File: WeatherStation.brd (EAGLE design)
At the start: 30.5 x 53.3 mm, 35 parts, among them J1 EDISON_CONNECTOR_FULLMOUNTING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, J2 EDISON_CONNECTOR_FULLHEADER, U1 MCP73831, U2 HTU21DSMD, U3 MPL3115A2LGA8, U4 PCA9306

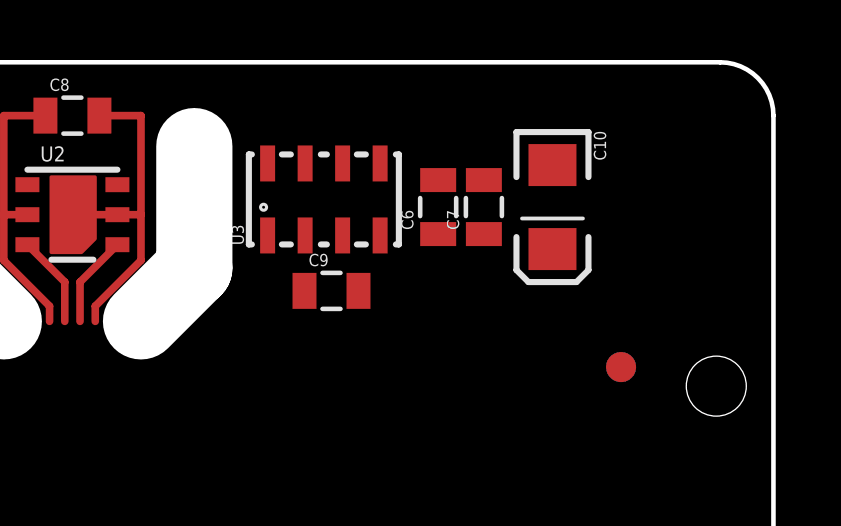
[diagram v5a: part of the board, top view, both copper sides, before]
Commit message: set and drew traces for MPL3115A2
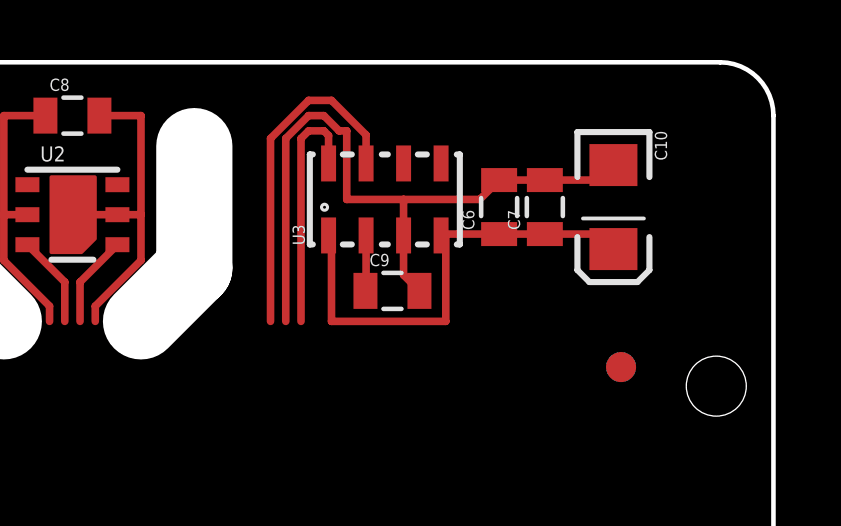
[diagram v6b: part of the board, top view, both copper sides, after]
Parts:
- moved C9 2.03 mm to (17.8, 45.7)
- moved C10 2.03 mm to (25.1, 48.5)
- moved C6 2.03 mm to (21.3, 48.5)
- moved C7 2.03 mm to (22.9, 48.5)
- moved U3 2.03 mm to (17.5, 48.8)
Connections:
- removed net N$10: U3.7
- removed net N$9: U3.8
- net SCL: now also U3.8
- net SDA: now also U3.7
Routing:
- net GND: track 11.2 -> 34.7 mm
- net 3.3V: track 15.7 -> 31.4 mm
- net SDA: track 3.07 -> 14.3 mm
- net SCL: track 3.07 -> 11.2 mm
- net N$3: track 0.00 -> 1.86 mm
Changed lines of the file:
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@@
 <element name="JP2" library="SparkFun-Connectors" package="1X02" value="M02PTH" x="2.032" y="22.098" smashed="yes" rot="R270"/>
 <element name="U2" library="SparkFun-Sensors" package="HTU21D" value="HTU21DSMD" x="7.112" y="48.26"/>
-<element name="U3" library="SparkFun-Sensors" package="LGA8" value="MPL3115A2LGA8" x="15.494" y="48.768" rot="R90"/>
+<element name="U3" library="SparkFun-Sensors" package="LGA8" value="MPL3115A2LGA8" x="17.526" y="48.768" rot="R90"/>
 <element name="U4" library="SparkFun-DigitalIC" package="PSOP-8" value="PCA9306" x="12.954" y="35.052">
 <attribute name="PROD_ID" value="IC-10023" x="12.954" y="35.052" size="1.778" layer="27" display="off"/>
@@
 <element name="C4" library="SparkFun-Capacitors" package="0805" value="4.7µF" x="11.176" y="27.94"/>
 <element name="C5" library="SparkFun-Capacitors" package="0805" value="4.7µF" x="14.986" y="25.4" rot="R90"/>
-<element name="C6" library="SparkFun-Capacitors" package="0805" value="0.1µF" x="19.304" y="48.514" rot="R90"/>
-<element name="C7" library="SparkFun-Capacitors" package="0805" value="1µF" x="20.828" y="48.514" rot="R90"/>
+<element name="C6" library="SparkFun-Capacitors" package="0805" value="0.1µF" x="21.336" y="48.514" rot="R90"/>
+<element name="C7" library="SparkFun-Capacitors" package="0805" value="1µF" x="22.86" y="48.514" rot="R90"/>
 <element name="R3" library="SparkFun-Resistors" package="0603-RES" value="330Ω" x="-33.782" y="-16.51"/>
 <element name="R4" library="SparkFun-Resistors" package="0603-RES" value="330Ω" x="-33.782" y="-19.558"/>
@@
 <element name="R7" library="SparkFun-Resistors" package="0603-RES" value="330Ω" x="-33.782" y="-28.702"/>
 <element name="C8" library="SparkFun-Capacitors" package="0805" value="4.7µF" x="7.112" y="51.562"/>
-<element name="C9" library="SparkFun-Capacitors" package="0805" value="0.1µF" x="15.748" y="45.72"/>
-<element name="C10" library="SparkFun-Capacitors" package="EIA3216" value="10µF" x="23.114" y="48.514" rot="R270"/>
+<element name="C9" library="SparkFun-Capacitors" package="0805" value="0.1µF" x="17.78" y="45.72"/>
+<element name="C10" library="SparkFun-Capacitors" package="EIA3216" value="10µF" x="25.146" y="48.514" rot="R270"/>
 </elements>
 <signals>
@@
 <wire x1="7.874" y1="45.212" x2="7.874" y2="44.704" width="0.254" layer="1"/>
 <wire x1="8.612" y1="48.26" x2="9.398" y2="48.26" width="0.254" layer="1"/>
-<wire x1="20.828" y1="49.414" x2="23.114" y2="49.914" width="0" layer="19" extent="1-1"/>
-<wire x1="19.304" y1="49.414" x2="20.828" y2="49.414" width="0" layer="19" extent="1-1"/>
-<wire x1="16.119" y1="47.568" x2="19.304" y2="49.414" width="0" layer="19" extent="1-1"/>
-<wire x1="16.648" y1="45.72" x2="16.119" y2="47.568" width="0" layer="19" extent="1-1"/>
-<wire x1="9.398" y1="48.26" x2="16.119" y2="47.568" width="0" layer="19" extent="1-1"/>
-<wire x1="13.724" y1="33.682" x2="16.648" y2="45.72" width="0" layer="19" extent="1-1"/>
+<wire x1="8.612" y1="48.26" x2="7.112" y2="48.26" width="0.254" layer="1"/>
+<wire x1="18.68" y1="45.72" x2="18.151" y2="46.249" width="0.254" layer="1"/>
+<wire x1="18.151" y1="46.249" x2="18.151" y2="47.568" width="0.254" layer="1"/>
+<wire x1="18.151" y1="47.568" x2="18.151" y2="48.768" width="0.254" layer="1"/>
+<wire x1="18.151" y1="48.768" x2="20.69" y2="48.768" width="0.254" layer="1"/>
+<wire x1="20.69" y1="48.768" x2="21.336" y2="49.414" width="0.254" layer="1"/>
+<wire x1="13.724" y1="33.682" x2="18.68" y2="45.72" width="0" layer="19" extent="1-1"/>
 <wire x1="12.076" y1="27.94" x2="13.724" y2="33.682" width="0" layer="19" extent="1-1"/>
 <wire x1="14.986" y1="26.3" x2="12.076" y2="27.94" width="0" layer="19" extent="1-1"/>
@@
 <wire x1="27.1272" y1="20.5232" x2="25.96" y2="20.58" width="0" layer="19" extent="16-16"/>
 <wire x1="28.2448" y1="22.1742" x2="26.9438" y2="22.1798" width="0" layer="19" extent="1-1"/>
-<wire x1="8.612" y1="48.26" x2="7.112" y2="48.26" width="0.254" layer="1"/>
+<wire x1="22.86" y1="49.414" x2="21.336" y2="49.414" width="0.254" layer="1"/>
+<wire x1="22.86" y1="49.414" x2="24.646" y2="49.414" width="0.254" layer="1"/>
+<wire x1="24.646" y1="49.414" x2="25.146" y2="49.914" width="0.254" layer="1"/>
+<wire x1="14.986" y1="48.768" x2="14.986" y2="44.704" width="0" layer="19" extent="1-16"/>
+<wire x1="14.986" y1="44.704" x2="9.398" y2="46.736" width="0" layer="19" extent="1-16"/>
+<wire x1="18.151" y1="48.768" x2="16.256" y2="48.768" width="0.254" layer="1"/>
+<wire x1="16.256" y1="48.768" x2="16.256" y2="51.054" width="0.254" layer="1"/>
+<wire x1="16.256" y1="51.054" x2="16.002" y2="51.054" width="0.254" layer="1"/>
+<wire x1="16.002" y1="51.054" x2="15.494" y2="51.562" width="0.254" layer="1"/>
+<wire x1="15.494" y1="51.562" x2="14.986" y2="51.562" width="0.254" layer="1"/>
+<wire x1="14.986" y1="51.562" x2="14.224" y2="50.8" width="0.254" layer="1"/>
+<wire x1="14.224" y1="50.8" x2="14.224" y2="44.704" width="0.254" layer="1"/>
+<wire x1="14.224" y1="44.704" x2="9.398" y2="46.736" width="0" layer="19" extent="1-16"/>
 </signal>
 <signal name="VSYS">
@@
 <wire x1="4.826" y1="46.736" x2="6.35" y2="45.212" width="0.254" layer="1"/>
 <wire x1="5.612" y1="48.26" x2="4.826" y2="48.26" width="0.254" layer="1"/>
-<wire x1="20.828" y1="47.614" x2="23.114" y2="47.114" width="0" layer="19" extent="1-1"/>
-<wire x1="19.304" y1="47.614" x2="20.828" y2="47.614" width="0" layer="19" extent="1-1"/>
-<wire x1="17.369" y1="47.568" x2="19.304" y2="47.614" width="0" layer="19" extent="1-1"/>
-<wire x1="13.619" y1="47.568" x2="17.369" y2="47.568" width="0" layer="19" extent="1-1"/>
-<wire x1="6.096" y1="45.466" x2="13.619" y2="47.568" width="0" layer="19" extent="1-1"/>
+<wire x1="6.35" y1="45.212" x2="6.35" y2="44.704" width="0.254" layer="1"/>
+<wire x1="19.401" y1="47.568" x2="19.447" y2="47.614" width="0.254" layer="1"/>
+<wire x1="19.447" y1="47.614" x2="21.336" y2="47.614" width="0.254" layer="1"/>
+<wire x1="21.336" y1="47.614" x2="22.86" y2="47.614" width="0.254" layer="1"/>
+<wire x1="22.86" y1="47.614" x2="24.646" y2="47.614" width="0.254" layer="1"/>
+<wire x1="24.646" y1="47.614" x2="25.146" y2="47.114" width="0.254" layer="1" curve="-90"/>
+<wire x1="15.651" y1="47.568" x2="15.748" y2="47.471" width="0.254" layer="1"/>
+<wire x1="15.748" y1="47.471" x2="15.748" y2="44.704" width="0.254" layer="1"/>
+<wire x1="15.748" y1="44.704" x2="19.558" y2="44.704" width="0.254" layer="1"/>
+<wire x1="19.558" y1="44.704" x2="19.558" y2="47.568" width="0.254" layer="1"/>
+<wire x1="19.558" y1="47.568" x2="19.401" y2="47.568" width="0.254" layer="1"/>
+<wire x1="6.35" y1="44.704" x2="15.748" y2="44.704" width="0" layer="19" extent="1-1"/>
+<wire x1="10.276" y1="27.94" x2="15.748" y2="44.704" width="0" layer="19" extent="1-1"/>
 <wire x1="12.4761" y1="26.35" x2="10.276" y2="27.94" width="0" layer="19" extent="1-1"/>
 <wire x1="21.717" y1="22.0472" x2="12.4761" y2="26.35" width="0" layer="19" extent="1-1"/>
-<wire x1="6.096" y1="45.466" x2="6.35" y2="45.212" width="0" layer="19" extent="1-16"/>
-<wire x1="6.35" y1="45.212" x2="6.35" y2="44.704" width="0.254" layer="1"/>
-<wire x1="6.35" y1="44.704" x2="13.619" y2="47.568" width="0" layer="19" extent="1-16"/>
 </signal>
 <signal name="GP183_PWM3">
@@
 <wire x1="8.612" y1="47.26" x2="7.366" y2="46.014" width="0.254" layer="1"/>
 <wire x1="7.366" y1="46.014" x2="7.366" y2="44.704" width="0.254" layer="1"/>
-<wire x1="7.366" y1="44.704" x2="13.224" y2="33.682" width="0" layer="19" extent="1-16"/>
+<contactref element="U3" pad="7"/>
+<wire x1="13.224" y1="33.682" x2="7.366" y2="44.704" width="0" layer="19" extent="1-1"/>
+<wire x1="16.901" y1="49.968" x2="16.901" y2="50.917" width="0.254" layer="1"/>
+<wire x1="16.901" y1="50.917" x2="15.748" y2="52.07" width="0.254" layer="1"/>
+<wire x1="15.748" y1="52.07" x2="14.986" y2="52.07" width="0.254" layer="1"/>
+<wire x1="14.986" y1="52.07" x2="13.716" y2="50.8" width="0.254" layer="1"/>
+<wire x1="13.716" y1="50.8" x2="13.716" y2="44.704" width="0.254" layer="1"/>
+<wire x1="13.716" y1="44.704" x2="8.612" y2="47.26" width="0" layer="19" extent="1-16"/>
 </signal>
 <signal name="SCL">
@@
 <wire x1="5.612" y1="47.26" x2="6.858" y2="46.014" width="0.254" layer="1"/>
 <wire x1="6.858" y1="46.014" x2="6.858" y2="44.704" width="0.254" layer="1"/>
-<wire x1="6.858" y1="44.704" x2="12.724" y2="33.682" width="0" layer="19" extent="1-16"/>
+<contactref element="U3" pad="8"/>
+<wire x1="12.724" y1="33.682" x2="6.858" y2="44.704" width="0" layer="19" extent="1-1"/>
+<wire x1="15.651" y1="49.968" x2="15.651" y2="50.897" width="0.254" layer="1"/>
+<wire x1="15.651" y1="50.897" x2="15.494" y2="51.054" width="0.254" layer="1"/>
+<wire x1="15.494" y1="51.054" x2="14.986" y2="51.054" width="0.254" layer="1"/>
+<wire x1="14.986" y1="51.054" x2="14.732" y2="50.8" width="0.254" layer="1"/>
+<wire x1="14.732" y1="50.8" x2="14.732" y2="44.704" width="0.254" layer="1"/>
+<wire x1="14.732" y1="44.704" x2="6.858" y2="44.704" width="0" layer="19" extent="1-16"/>
 </signal>
 <signal name="N$3">
 <contactref element="U3" pad="2"/>
 <contactref element="C9" pad="1"/>
-<wire x1="14.869" y1="47.568" x2="14.848" y2="45.72" width="0" layer="19" extent="1-1"/>
-</signal>
-<signal name="N$9">
-<contactref element="U3" pad="8"/>
-</signal>
-<signal name="N$10">
-<contactref element="U3" pad="7"/>
+<wire x1="16.88" y1="45.72" x2="16.901" y2="45.741" width="0.254" layer="1"/>
+<wire x1="16.901" y1="45.741" x2="16.901" y2="47.568" width="0.254" layer="1"/>
 </signal>
 </signals>

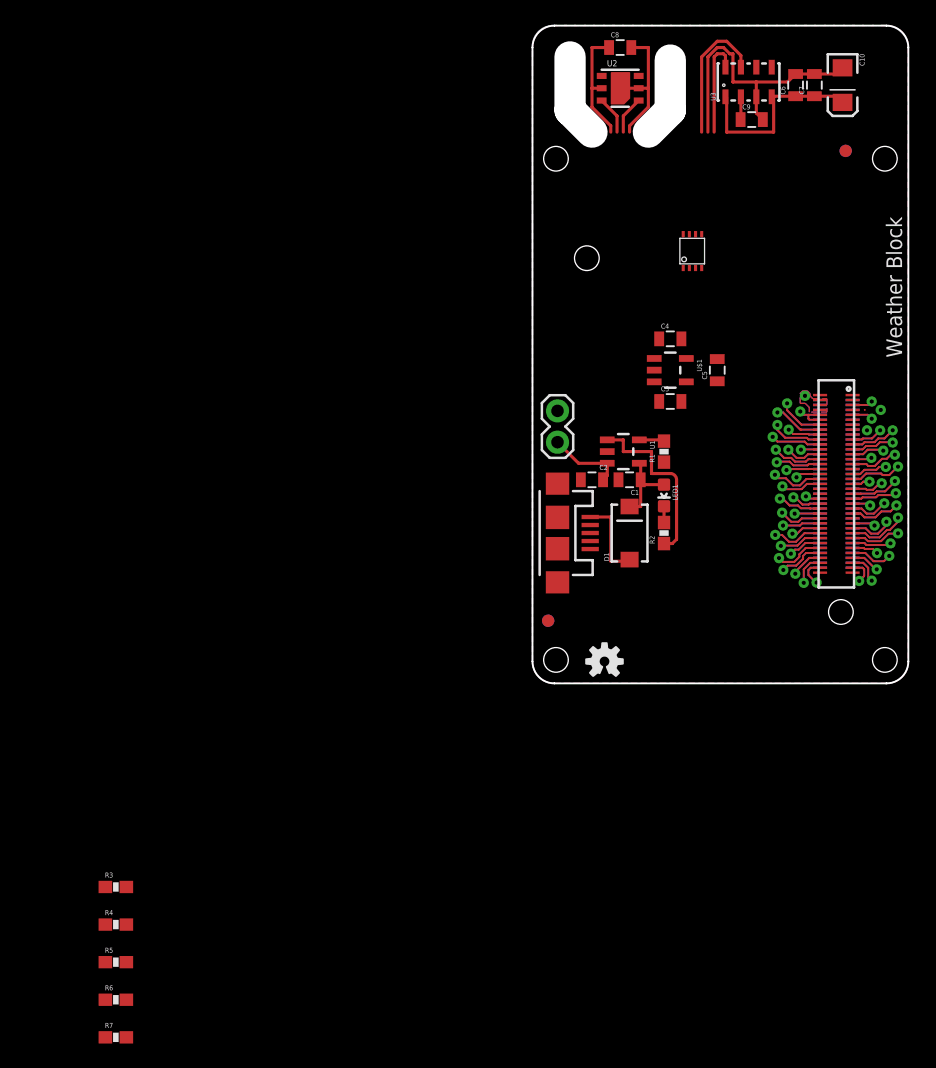
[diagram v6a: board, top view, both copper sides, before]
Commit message: set and drew traces for MIC5205
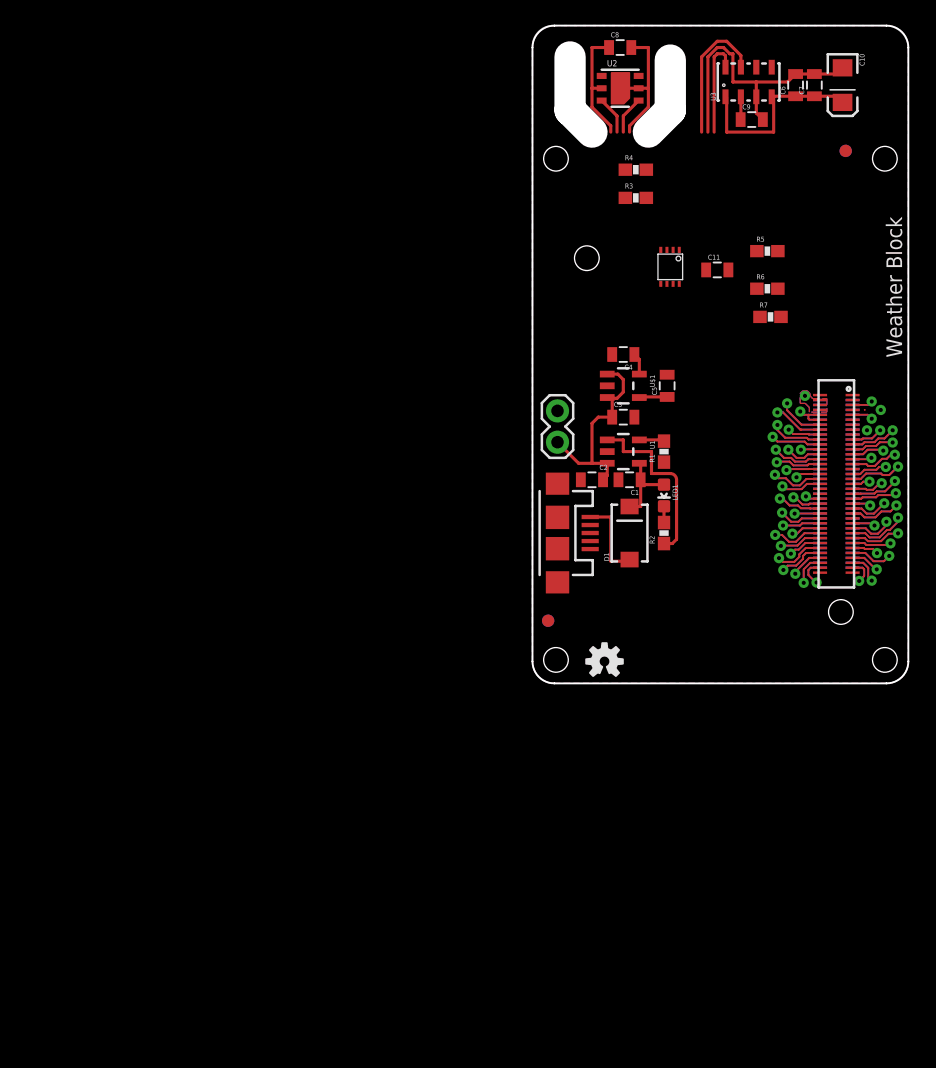
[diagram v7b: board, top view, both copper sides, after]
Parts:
- added C11: 4.7µF, SparkFun-Capacitors:0805
- R3, R4, R5, R6, R7: value 330Ω -> 1kΩ
- moved R7 78.9 mm to (19.3, 29.7)
- moved R5 78.2 mm to (19.1, 35.1)
- moved R6 78.2 mm to (19.1, 32.0)
- moved R4 74.3 mm to (8.38, 41.7)
- moved R3 70.0 mm to (8.38, 39.4)
- moved C5 4.26 mm to (10.9, 24.1)
- moved C3 4.02 mm to (7.37, 21.6)
- moved C4 4.02 mm to (7.37, 26.7), turned to 180 degrees
- moved U$1 4.02 mm to (7.37, 24.1)
- moved U4 2.18 mm to (11.2, 33.8), turned to 180 degrees
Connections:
- removed net N$7: C3.1, U$1.1, U$1.3
- new net N$10: C11.1, R5.1, U4.7, U4.8
- new net N$11: R6.2, U4.6
- new net N$12: R7.2, U4.5
- net 1.8V: now also R5.2, R6.1, R7.1
- net 3.3V: now also R3.1, R4.1, U4.1
- net GND: now also C11.2
- net SCL: now also R3.2
- net SDA: now also R4.2
- net VBAT: now also C3.1, U$1.1, U$1.3
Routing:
- net VBAT: track 6.22 -> 17.3 mm
- net N$8: track 0.00 -> 2.28 mm
- net 3.3V: track 31.4 -> 33.1 mm

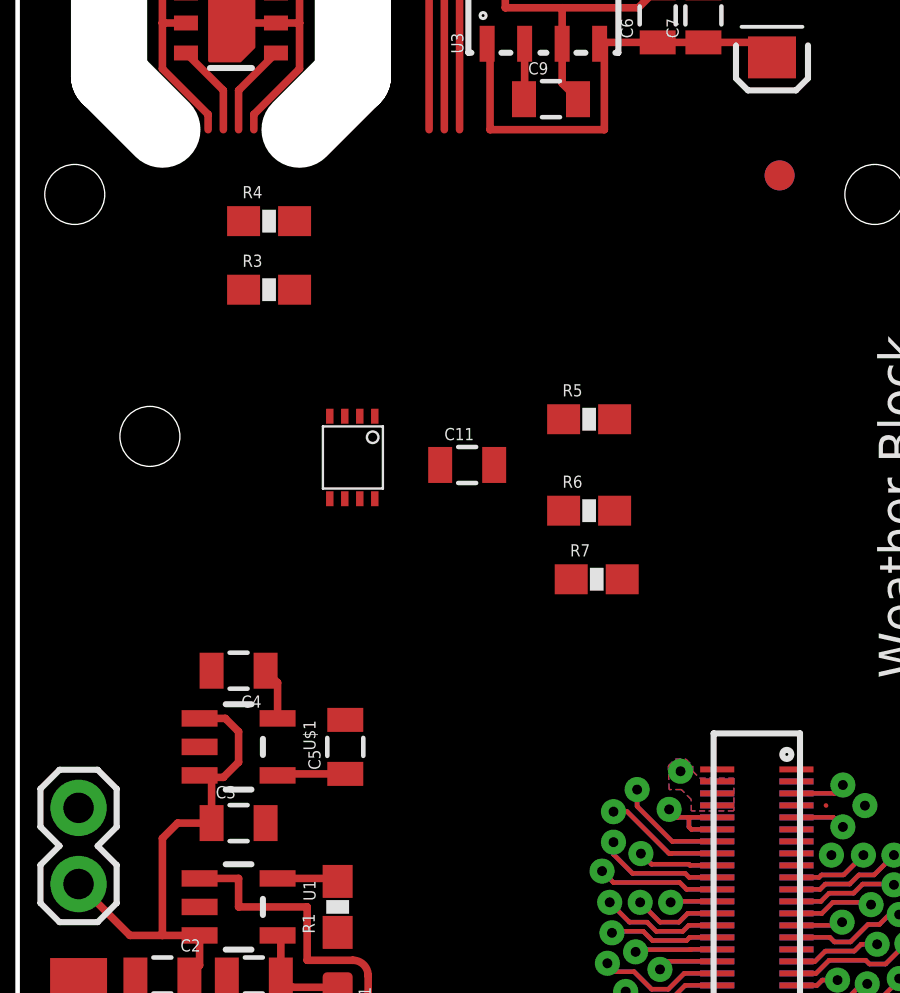
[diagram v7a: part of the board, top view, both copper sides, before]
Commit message: drew traces for PCA9306
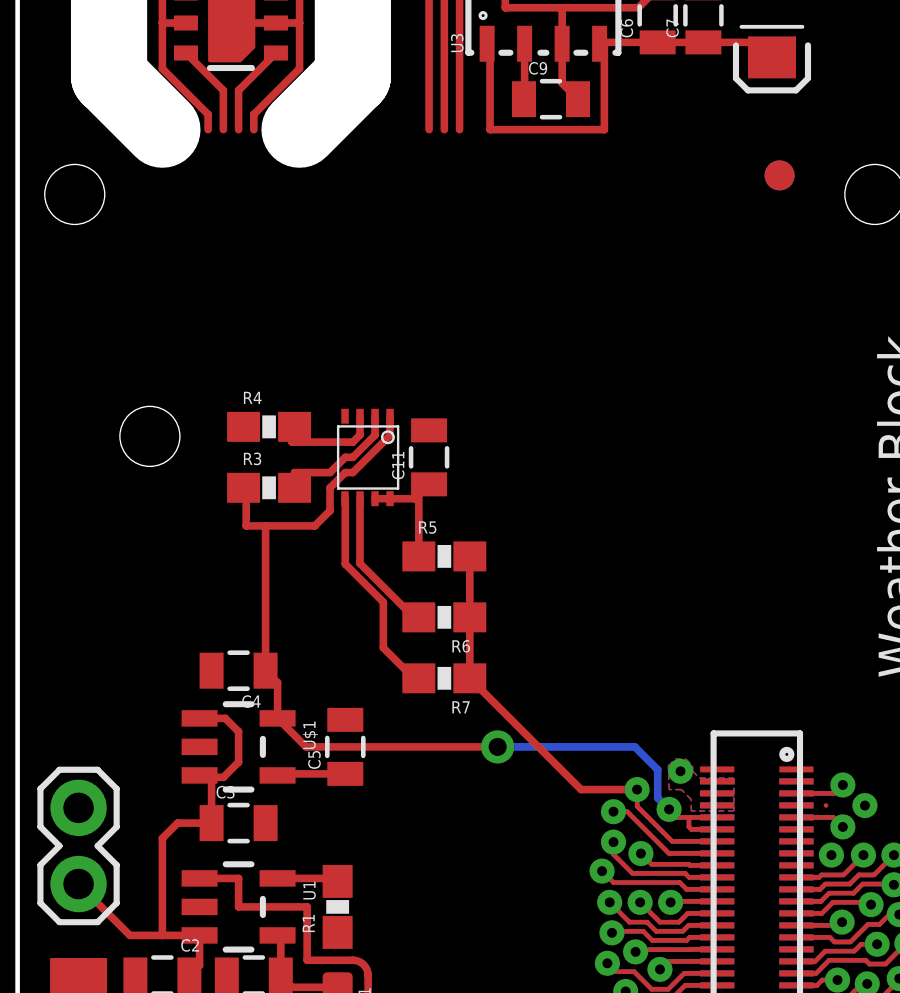
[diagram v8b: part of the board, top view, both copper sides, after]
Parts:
- moved R4 6.86 mm to (8.38, 34.8)
- moved R5 6.65 mm to (14.2, 30.5)
- moved R3 6.60 mm to (8.38, 32.8)
- moved R7 6.06 mm to (14.2, 26.4), turned to 180 degrees
- moved R6 5.99 mm to (14.2, 28.4), turned to 180 degrees
- moved C11 1.30 mm to (13.7, 33.8), turned to 90 degrees
- moved U4 0.51 mm to (11.7, 33.8)
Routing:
- net 3.3V: track 33.1 -> 61.3 mm, vias 1 -> 2
- net 1.8V: track 7.43 -> 18.6 mm
- net N$12: track 0.00 -> 7.10 mm
- net N$11: track 0.00 -> 4.86 mm
- net N$10: track 0.00 -> 4.54 mm
- net SCL: track 11.2 -> 15.5 mm
- net SDA: track 14.3 -> 17.8 mm
